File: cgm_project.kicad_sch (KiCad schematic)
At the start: 32 parts, among them J1 JST BATT CONNECTOR, J2 USB_C_Receptacle_USB2.0_16P, Q1 AO3400, SW1 SW_SPDT, SW2 BOOT, SW3 SW_Push, U1 TP4056-42-ESOP8, U2 AP2112K-3.3, U3 ESP32-C3-WROOM-02, U4 OPA380

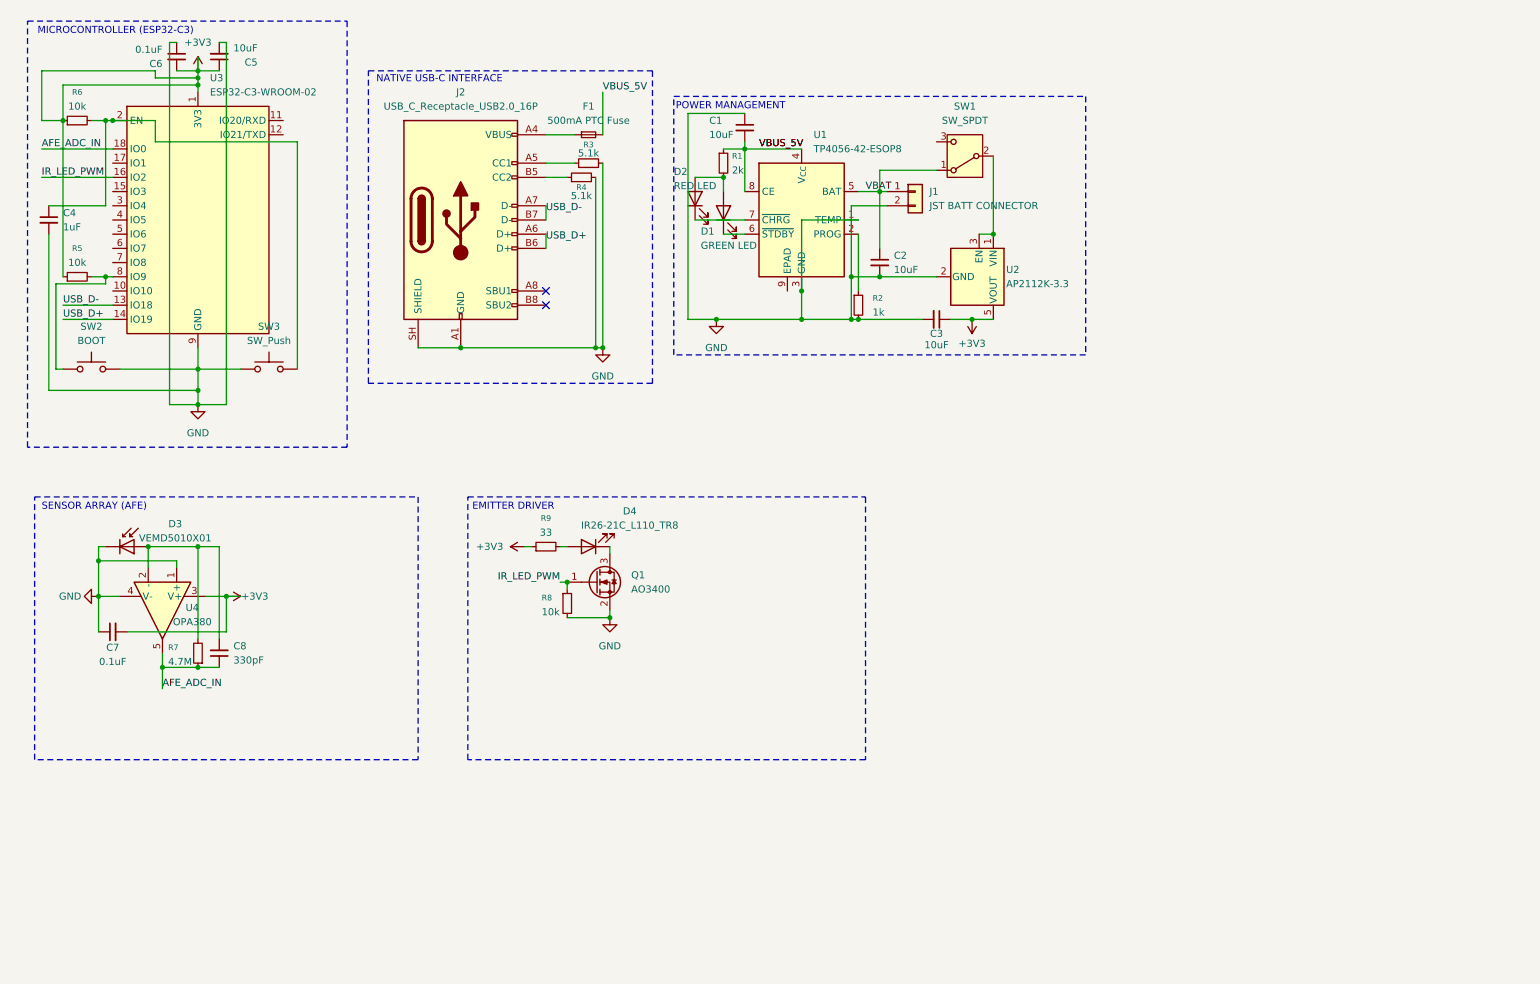
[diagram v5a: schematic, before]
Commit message: fix: resolve ERC power flag collisions, clear unused pin warning
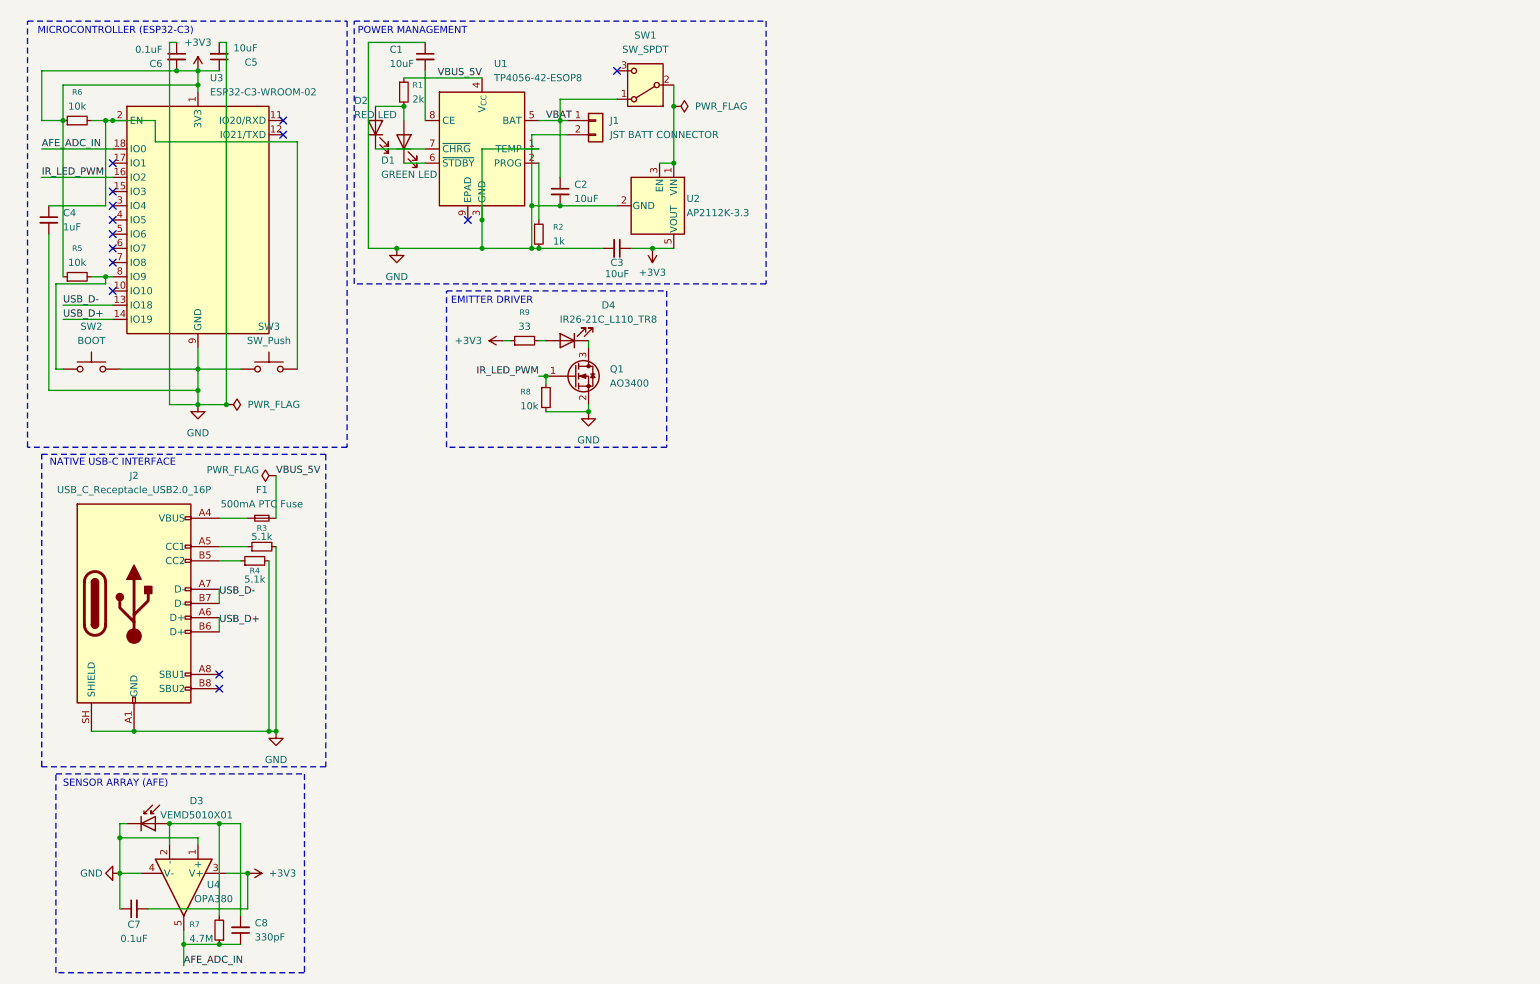
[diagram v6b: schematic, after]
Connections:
- net VBUS_5V: no longer C1.2, U1.8 (CE)
- new net: C1.2, U1.8 (CE)
- no-connect marks 2 -> 14
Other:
- moved on the sheet: C1, C2, C3, C7, C8, D1, D2, D3, D4, F1, J1, J2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

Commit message: chore: assign physical footprint for all schematic component
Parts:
- C1, C2, C3, C4, C5, C6, C7, C8: footprint (none) -> Capacitor_SMD:C_0805_2012Metric
- D1, D2, D3: footprint (none) -> LED_SMD:LED_0805_2012Metric
- F1: footprint (none) -> Fuse:Fuse_1206_3216Metric
- J1: footprint (none) -> Connector_JST:JST_PH_S2B-PH-K_1x02_P2.00mm_Horizontal
- J2: footprint (none) -> Connector_USB:USB_C_Receptacle_HCTL_HC-TYPE-C-16P-01A
- Q1: footprint (none) -> Package_TO_SOT_SMD:SOT-23
- R1, R2, R3, R4, R5, R6, R7, R8, R9: footprint (none) -> Resistor_SMD:R_0805_2012Metric
- SW1: footprint (none) -> Button_Switch_SMD:SW_SPDT_PCM12
- SW2, SW3: footprint (none) -> Button_Switch_SMD:SW_SPST_FSMSM
- U4: footprint (none) -> Package_SO:SOIC-8-1EP_3.9x4.9mm_P1.27mm_EP2.29x3mm
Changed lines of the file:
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@@
 			)
 		)
-		(property "Footprint" ""
+		(property "Footprint" "Resistor_SMD:R_0805_2012Metric"
 			(at 55.88 111.76 0)
 			(hide yes)
@@
 			)
 		)
-		(property "Footprint" ""
+		(property "Footprint" "Fuse:Fuse_1206_3216Metric"
 			(at 57.15 104.14 0)
 			(hide yes)
@@
 			)
 		)
-		(property "Footprint" ""
+		(property "Footprint" "Button_Switch_SMD:SW_SPST_FSMSM"
 			(at 26.67 72.39 0)
 			(hide yes)
@@
 			)
 		)
-		(property "Footprint" ""
+		(property "Footprint" "LED_SMD:LED_0805_2012Metric"
 			(at 82.55 36.83 0)
 			(hide yes)
@@
 			)
 		)
-		(property "Footprint" ""
+		(property "Footprint" "Package_SO:SOIC-8-1EP_3.9x4.9mm_P1.27mm_EP2.29x3mm"
 			(at 43.18 170.18 0)
 			(hide yes)
@@
 			)
 		)
-		(property "Footprint" ""
+		(property "Footprint" "Resistor_SMD:R_0805_2012Metric"
 			(at 49.53 177.8 0)
 			(hide yes)
@@
 			)
 		)
-		(property "Footprint" ""
+		(property "Footprint" "Resistor_SMD:R_0805_2012Metric"
 			(at 107.95 82.55 0)
 			(hide yes)
@@
 			)
 		)
-		(property "Footprint" ""
+		(property "Footprint" "Capacitor_SMD:C_0805_2012Metric"
 			(at 53.34 177.8 0)
 			(hide yes)
@@
 			)
 		)
-		(property "Footprint" ""
+		(property "Footprint" "Resistor_SMD:R_0805_2012Metric"
 			(at 24.13 60.96 0)
 			(hide yes)
@@
 			)
 		)
-		(property "Footprint" ""
+		(property "Footprint" "Connector_JST:JST_PH_S2B-PH-K_1x02_P2.00mm_Horizontal"
 			(at 116.84 33.02 0)
 			(hide yes)
@@
 			)
 		)
-		(property "Footprint" ""
+		(property "Footprint" "Capacitor_SMD:C_0805_2012Metric"
 			(at 86.36 21.59 0)
 			(hide yes)
@@
 			)
 		)
-		(property "Footprint" ""
+		(property "Footprint" "Capacitor_SMD:C_0805_2012Metric"
 			(at 19.05 50.8 0)
 			(hide yes)
@@
 			)
 		)
-		(property "Footprint" ""
+		(property "Footprint" "Capacitor_SMD:C_0805_2012Metric"
 			(at 110.49 45.72 0)
 			(hide yes)
@@
 			)
 		)
-		(property "Footprint" ""
+		(property "Footprint" "Resistor_SMD:R_0805_2012Metric"
 			(at 106.68 53.34 0)
 			(hide yes)
@@
 			)
 		)
-		(property "Footprint" ""
+		(property "Footprint" "Capacitor_SMD:C_0805_2012Metric"
 			(at 34.29 173.99 0)
 			(hide yes)
@@
 			)
 		)
-		(property "Footprint" ""
+		(property "Footprint" "Capacitor_SMD:C_0805_2012Metric"
 			(at 120.65 55.88 0)
 			(hide yes)
@@
 			)
 		)
-		(property "Footprint" ""
+		(property "Footprint" "Connector_USB:USB_C_Receptacle_HCTL_HC-TYPE-C-16P-01A"
 			(at 38.1 119.38 0)
 			(hide yes)
@@
 			)
 		)
-		(property "Footprint" ""
+		(property "Footprint" "Capacitor_SMD:C_0805_2012Metric"
 			(at 41.91 21.59 0)
 			(hide yes)
@@
 			)
 		)
-		(property "Footprint" ""
+		(property "Footprint" "LED_SMD:LED_0805_2012Metric"
 			(at 77.47 34.29 0)
 			(hide yes)
@@
 			)
 		)
-		(property "Footprint" ""
+		(property "Footprint" "Resistor_SMD:R_0805_2012Metric"
 			(at 57.15 109.22 0)
 			(hide yes)
@@
 			)
 		)
-		(property "Footprint" ""
+		(property "Footprint" "Package_TO_SOT_SMD:SOT-23"
 			(at 118.11 76.2 0)
 			(hide yes)
@@
 			)
 		)
-		(property "Footprint" ""
+		(property "Footprint" "Resistor_SMD:R_0805_2012Metric"
 			(at 82.55 27.94 0)
 			(hide yes)
@@
 			)
 		)
-		(property "Footprint" ""
+		(property "Footprint" "LED_SMD:LED_0805_2012Metric"
 			(at 36.83 158.75 0)
 			(hide yes)
@@
 			)
 		)
-		(property "Footprint" ""
+		(property "Footprint" "Capacitor_SMD:C_0805_2012Metric"
 			(at 49.53 21.59 0)
 			(hide yes)
@@
 			)
 		)
-		(property "Footprint" ""
+		(property "Footprint" "Button_Switch_SMD:SW_SPDT_PCM12"
 			(at 125.73 26.67 0)
 			(hide yes)
@@
 			)
 		)
-		(property "Footprint" ""
+		(property "Footprint" "Resistor_SMD:R_0805_2012Metric"
 			(at 24.13 33.02 0)
 			(hide yes)
@@
 			)
 		)
-		(property "Footprint" ""
+		(property "Footprint" "Resistor_SMD:R_0805_2012Metric"
 			(at 104.14 72.39 0)
 			(hide yes)
@@
 			)
 		)
-		(property "Footprint" ""
+		(property "Footprint" "Button_Switch_SMD:SW_SPST_FSMSM"
 			(at 58.42 72.39 0)
 			(hide yes)

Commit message: feat: replace onboard IR LED with off-board wire connector
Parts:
- removed D4: IR26-21C_L110_TR8, LED_SMD:LED_1206_3216Metric, symbol LED:IR26-21C_L110_TR8
- added J3: Conn_01x02, symbol Connector_Generic:Conn_01x02
- SW3: value SW_Push -> RESET
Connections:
- net at Q1.3 (D): now also J3.2 (Pin_2)
- net at R9.2: now also J3.1 (Pin_1)
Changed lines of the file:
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@@
 	(wire
 		(pts
+			(xy 113.03 72.39) (xy 115.57 72.39)
+		)
+		(stroke
+			(width 0)
+			(type default)
+		)
+	)
+	(wire
+		(pts
 			(xy 45.72 73.66) (xy 45.72 77.47)
 		)
@@
 	(wire
 		(pts
-			(xy 106.68 72.39) (xy 107.95 72.39)
+			(xy 106.68 72.39) (xy 110.49 72.39)
 		)
 		(stroke
@@
 	)
 	(symbol
-		(lib_id "LED:IR26-21C_L110_TR8")
-		(at 111.76 72.39 180)
-		(unit 1)
-		(body_style 1)
-		(exclude_from_sim no)
-		(in_bom yes)
-		(on_board yes)
-		(in_pos_files yes)
-		(dnp no)
-		(property "Reference" "D4"
-			(at 119.126 66.04 0)
-			(show_name no)
-			(do_not_autoplace no)
-			(effects
-				(font
-					(size 1.27 1.27)
-				)
-			)
-		)
-		(property "Value" "IR26-21C_L110_TR8"
-			(at 119.126 68.58 0)
-			(show_name no)
-			(do_not_autoplace no)
-			(effects
-				(font
-					(size 1.27 1.27)
-				)
-			)
-		)
-		(property "Footprint" "LED_SMD:LED_1206_3216Metric"
-			(at 111.76 77.47 0)
-			(hide yes)
-			(show_name no)
-			(do_not_autoplace no)
-			(effects
-				(font
-					(size 1.27 1.27)
-				)
-			)
-		)
-		(property "Datasheet" "http://www.everlight.com/file/ProductFile/IR26-21C-L110-TR8.pdf"
-			(at 111.76 72.39 0)
-			(hide yes)
-			(show_name no)
-			(do_not_autoplace no)
-			(effects
-				(font
-					(size 1.27 1.27)
-				)
-			)
-		)
-		(property "Description" "940nm, 20 deg, Infrared LED, 1206"
-			(at 111.76 72.39 0)
-			(hide yes)
-			(show_name no)
-			(do_not_autoplace no)
-			(effects
-				(font
-					(size 1.27 1.27)
-				)
-			)
-		)
-		(pin "1"
-		)
-		(pin "2"
-		)
-		(instances
-			(project "cgm_project"
-				(path "/56312daa-544d-4a20-aa90-3dd296ddb5b0"
-					(reference "D4")
-					(unit 1)
-				)
-			)
-		)
-	)
-	(symbol
 		(lib_id "Device:C_Small")
 		(at 86.36 21.59 0)
@@
 	)
 	(symbol
+		(lib_id "Connector_Generic:Conn_01x02")
+		(at 110.49 67.31 90)
+		(unit 1)
+		(body_style 1)
+		(exclude_from_sim no)
+		(in_bom yes)
+		(on_board yes)
+		(in_pos_files yes)
+		(dnp no)
+		(fields_autoplaced yes)
+		(property "Reference" "J3"
+			(at 115.57 66.0399 90)
+			(show_name no)
+			(do_not_autoplace no)
+			(effects
+				(font
+					(size 1.27 1.27)
+				)
+				(justify right)
+			)
+		)
+		(property "Value" "Conn_01x02"
+			(at 115.57 68.5799 90)
+			(show_name no)
+			(do_not_autoplace no)
+			(effects
+				(font
+					(size 1.27 1.27)
+				)
+				(justify right)
+			)
+		)
+		(property "Footprint" ""
+			(at 110.49 67.31 0)
+			(hide yes)
+			(show_name no)
+			(do_not_autoplace no)
+			(effects
+				(font
+					(size 1.27 1.27)
+				)
+			)
+		)
+		(property "Datasheet" ""
+			(at 110.49 67.31 0)
+			(hide yes)
+			(show_name no)
+			(do_not_autoplace no)
+			(effects
+				(font
+					(size 1.27 1.27)
+				)
+			)
+		)
+		(property "Description" "Generic connector, single row, 01x02, script generated (kicad-library-utils/schlib/autogen/connector/)"
+			(at 110.49 67.31 0)
+			(hide yes)
+			(show_name no)
+			(do_not_autoplace no)
+			(effects
+				(font
+					(size 1.27 1.27)
+				)
+			)
+		)
+		(pin "1"
+		)
+		(pin "2"
+		)
+		(instances
+			(project "cgm_project"
+				(path "/56312daa-544d-4a20-aa90-3dd296ddb5b0"
+					(reference "J3")
+					(unit 1)
+				)
+			)
+		)
+	)
+	(symbol
 		(lib_id "Device:D_Photo")
 		(at 38.1 158.75 0)
@@
 			)
 		)
-		(property "Value" "SW_Push"
+		(property "Value" "RESET"
 			(at 58.42 72.39 0)
 			(show_name no)
